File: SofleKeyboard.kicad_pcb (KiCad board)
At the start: 2 copper layers, 143.5 x 111.7 mm, 84 parts, among them J3 OLED, SW1 SW_PUSH_LED, SW10 SW_PUSH_LED, SW11 SW_PUSH_LED, SW12 SW_PUSH_LED, SW13 SW_PUSH_LED, SW14 SW_PUSH_LED, SW15 SW_PUSH_LED, SW16 SW_PUSH_LED, SW17 SW_PUSH_LED, SW18 SW_PUSH_LED, SW19 SW_PUSH_LED, SW2 SW_PUSH_LED, SW20 SW_PUSH_LED, SW21 SW_PUSH_LED, SW22 SW_PUSH_LED, SW23 SW_PUSH_LED, SW24 SW_PUSH_LED, SW26 SW_PUSH_LED, SW27 SW_PUSH_LED, SW28 SW_PUSH_LED, SW29 SW_PUSH_LED, SW3 SW_PUSH_LED, SW30 SW_PUSH_LED, SW4 SW_PUSH_LED, SW5 SW_PUSH_LED, SW6 SW_PUSH_LED, SW7 SW_PUSH_LED, SW8 SW_PUSH_LED, SW9 SW_PUSH_LED, U1 ProMicro

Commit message: update diode footprint, add ground zones, start board routing
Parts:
- D1, D10, D11, D12, D13, D14, D15, D16, D17, D18, D19, D2, D20, D21, D22, D23, D24, D26, D27, D28, D29, D3, D30, D4, D5, D6, D7, D8, D9: footprint Diode_SMD:crkbd-diode -> SofleChoc:crkbd-diode
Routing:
- net row0: track 0.00 -> 187.0 mm, vias 0 -> 6
- net row1: track 0.00 -> 177.8 mm, vias 0 -> 7
- net row4: track 0.00 -> 175.4 mm, vias 0 -> 6
- net Net-(SW_BATT+1-A): track 0.00 -> 111.1 mm, vias 0 -> 2
- net row2: track 0.00 -> 69.4 mm, vias 0 -> 1
- net row3: track 0.00 -> 69.0 mm, vias 0 -> 1
- net col6: track 0.00 -> 66.5 mm, vias 0 -> 1
- net ENCA: track 0.00 -> 64.9 mm, vias 0 -> 1
- net GND: track 0.00 -> 62.4 mm
- net ENCB: track 0.00 -> 61.7 mm, vias 0 -> 1
- net RESET: track 0.00 -> 60.1 mm, vias 0 -> 1
- net CS: track 0.00 -> 54.7 mm, vias 0 -> 5
- net SDA: track 0.00 -> 46.6 mm, vias 0 -> 4
- net SCL: track 0.00 -> 38.0 mm, vias 0 -> 3
- net VCC: track 0.00 -> 35.3 mm, vias 0 -> 1
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- added copper zone on B.Cu, net GND
- added copper zone on F.Cu, net GND

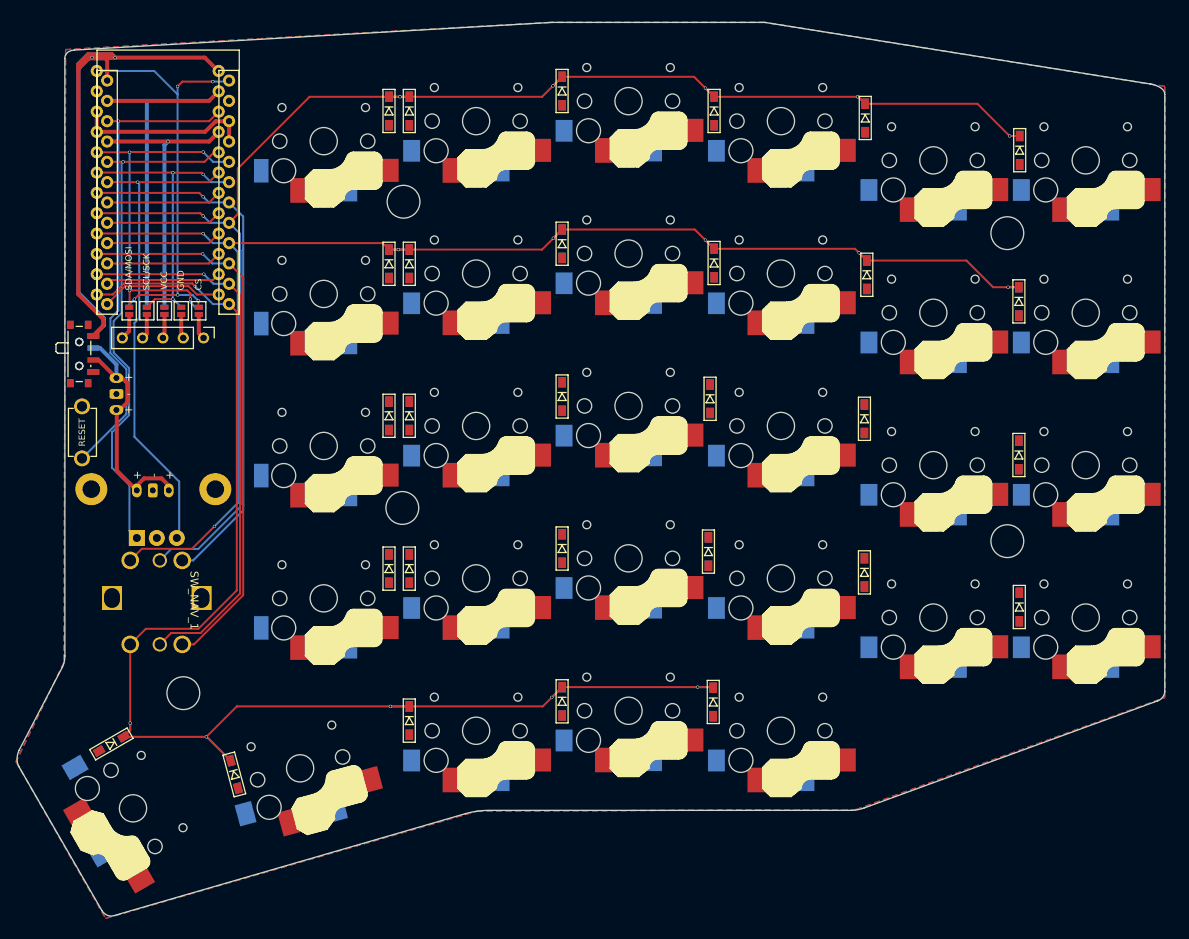
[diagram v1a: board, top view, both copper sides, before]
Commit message: wire columns 5, 4, 3 and 2
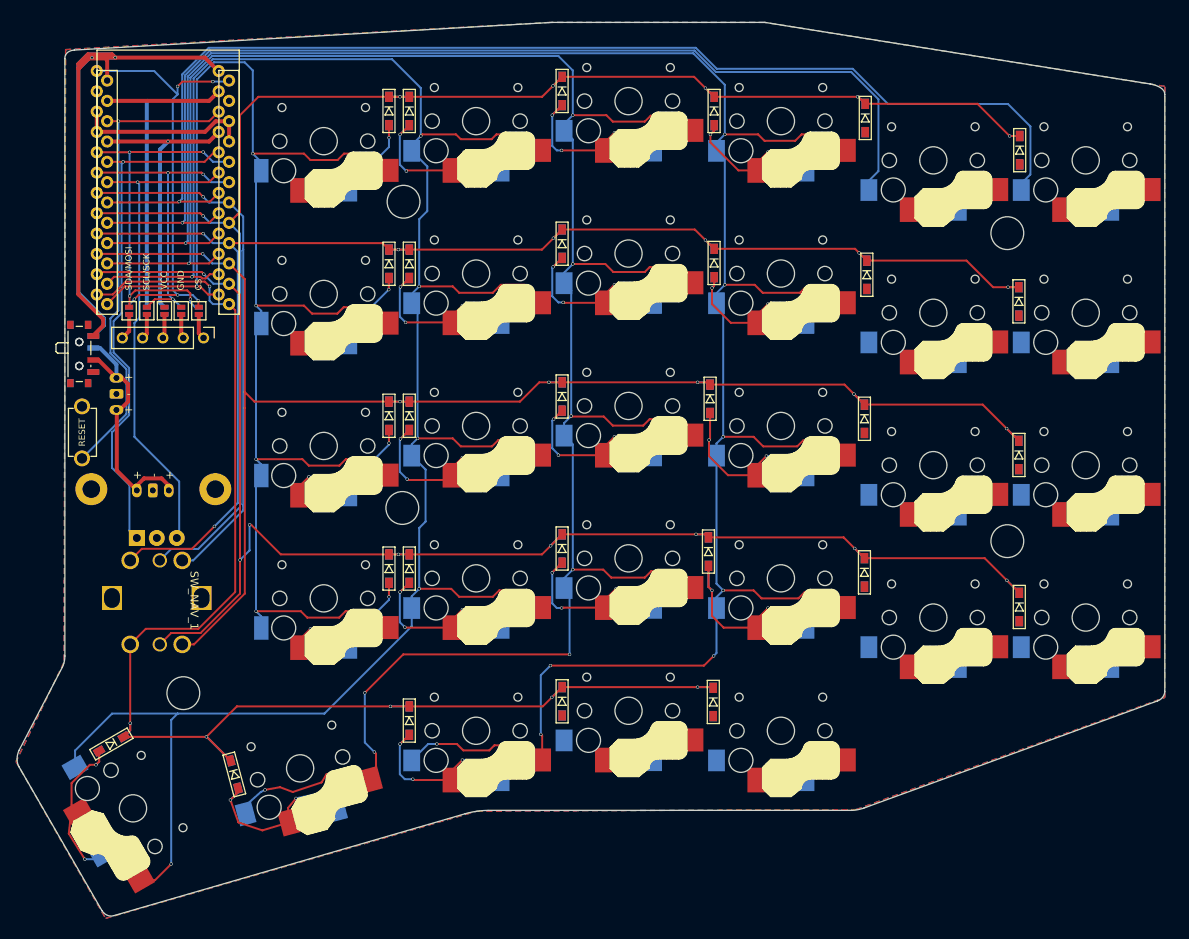
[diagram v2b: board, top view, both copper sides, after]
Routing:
- net col2: track 14.4 -> 298.8 mm, vias 0 -> 9
- net col3: track 14.4 -> 289.2 mm, vias 0 -> 9
- net col4: track 14.4 -> 283.9 mm, vias 0 -> 6
- net col5: track 15.3 -> 194.6 mm, vias 0 -> 5
- net col0: track 14.4 -> 150.4 mm, vias 0 -> 1
- net col1: track 14.4 -> 135.3 mm, vias 0 -> 1
- net row3: track 69.0 -> 186.1 mm, vias 1 -> 8
- net row2: track 69.4 -> 181.3 mm, vias 1 -> 6
- net Net-(D16-A): track 0.00 -> 25.1 mm, vias 0 -> 2
- net Net-(D22-A): track 0.00 -> 25.1 mm, vias 0 -> 2
- net Net-(D28-A): track 0.00 -> 23.4 mm, vias 0 -> 3
- net Net-(D14-A): track 0.00 -> 23.4 mm, vias 0 -> 3
- net Net-(D21-A): track 0.00 -> 23.2 mm, vias 0 -> 3
- net Net-(D2-A): track 0.00 -> 23.0 mm, vias 0 -> 3
- net Net-(D3-A): track 0.00 -> 23.0 mm, vias 0 -> 3
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
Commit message: first iteration done
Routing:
- net col1: track 135.3 -> 314.3 mm, vias 1 -> 9
- net col0: track 150.4 -> 325.1 mm, vias 1 -> 7
- net Net-(D23-A): track 0.00 -> 30.3 mm, vias 0 -> 2
- net Net-(D17-A): track 0.00 -> 30.2 mm, vias 0 -> 2
- net Net-(D5-A): track 0.00 -> 29.2 mm, vias 0 -> 2
- net Net-(D11-A): track 0.00 -> 27.7 mm, vias 0 -> 2
- net Net-(D30-A): track 0.00 -> 24.2 mm, vias 0 -> 2
- net Net-(D29-A): track 0.00 -> 24.0 mm, vias 0 -> 3
- net Net-(D18-A): track 0.00 -> 20.8 mm, vias 0 -> 2
- net Net-(D12-A): track 0.00 -> 20.8 mm, vias 0 -> 2
- net Net-(D6-A): track 0.00 -> 20.8 mm, vias 0 -> 2
- net Net-(D24-A): track 0.00 -> 20.5 mm, vias 0 -> 2
- net GND: track 62.4 -> 79.1 mm, vias 0 -> 9
- net Net-(J3-Pin_1): track 3.30 -> 6.60 mm
- net Net-(J3-Pin_5): track 3.20 -> 6.39 mm
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
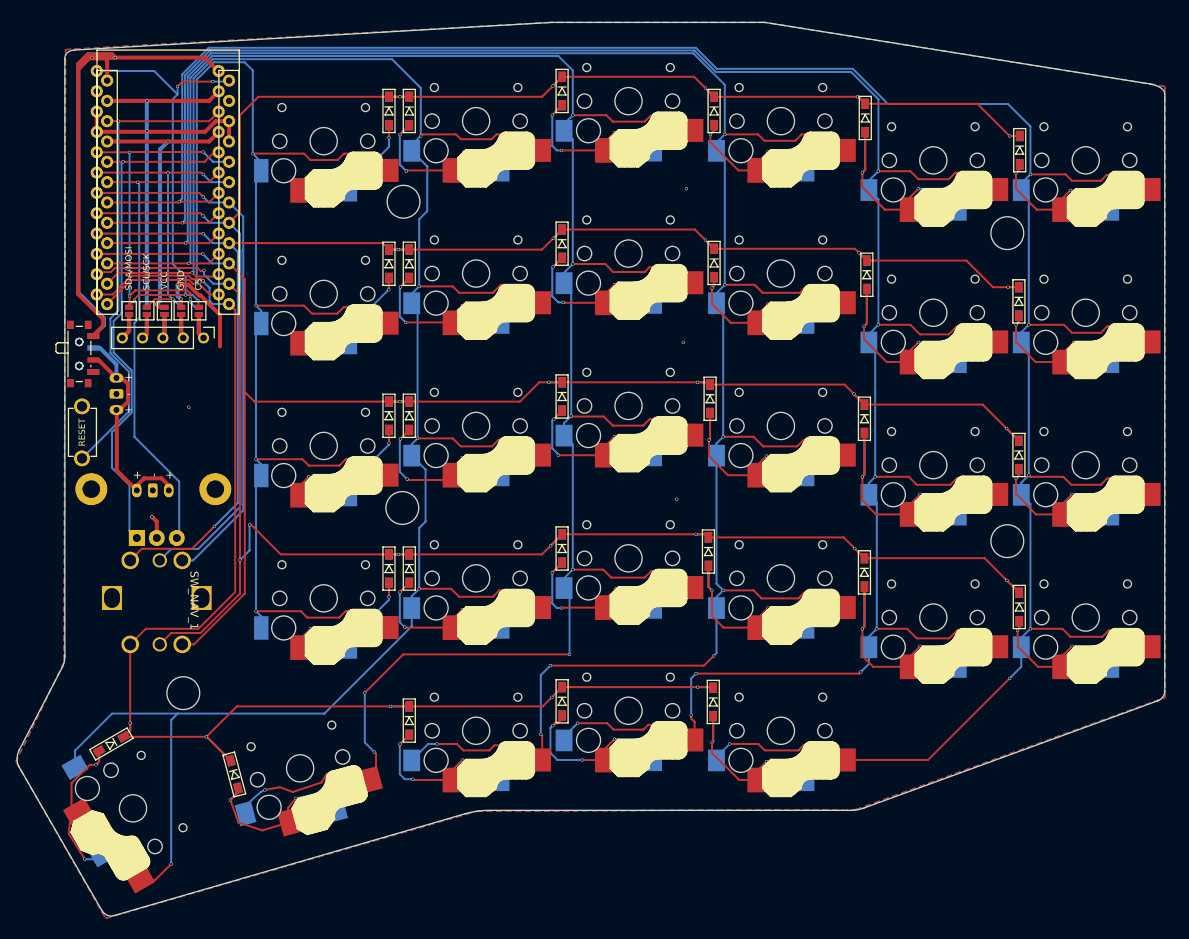
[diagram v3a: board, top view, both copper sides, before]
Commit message: add license
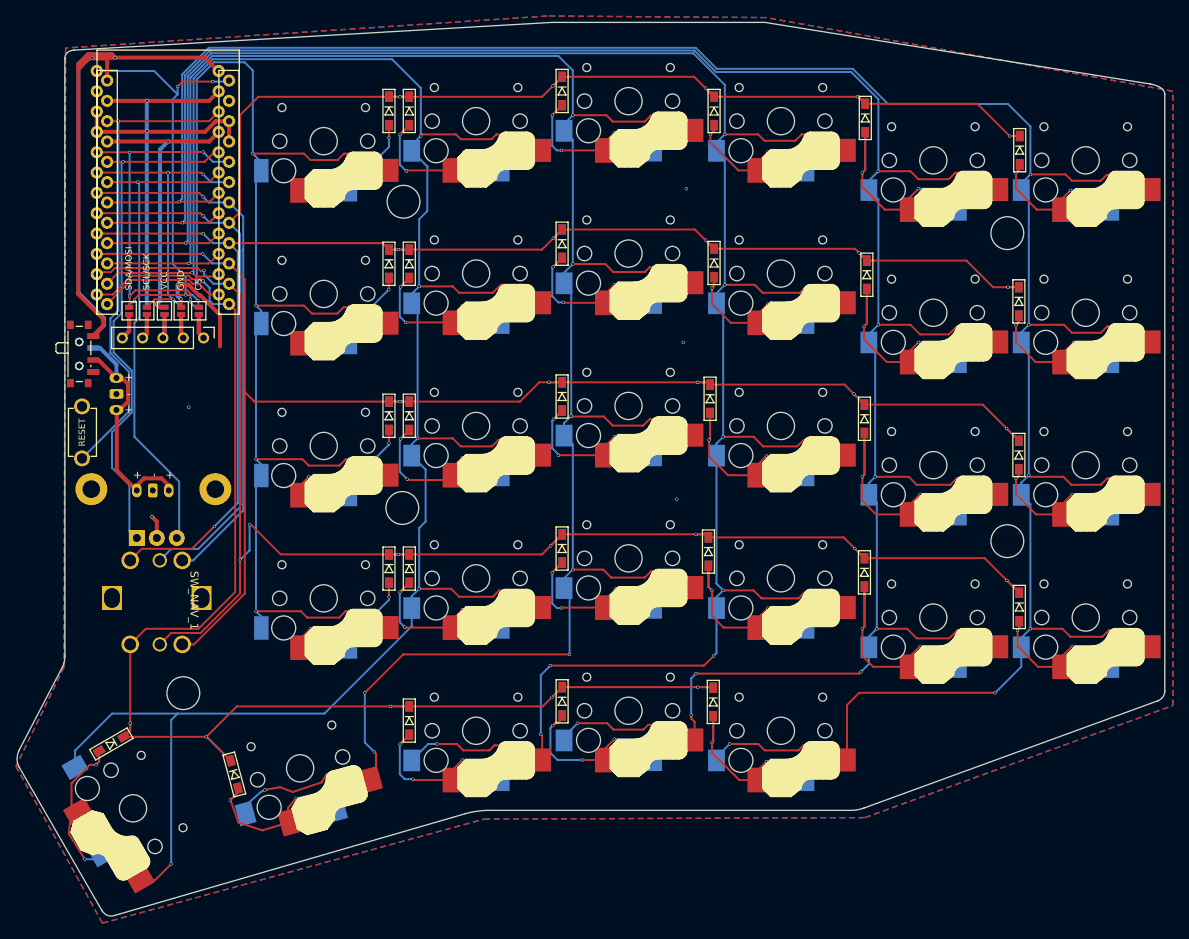
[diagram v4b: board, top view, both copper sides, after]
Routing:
- net col0: track 325.1 -> 329.1 mm
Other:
- rule pad_to_mask_clearance: 0.2 -> 0
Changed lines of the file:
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@@
 			(dielectric_constraints no)
 		)
-		(pad_to_mask_clearance 0.2)
+		(pad_to_mask_clearance 0)
 		(allow_soldermask_bridges_in_footprints no)
 		(tenting front back)
 		(grid_origin 150.33912 99.10264)
 		(pcbplotparams
-			(layerselection 0x00000000_00000000_55555555_575555ff)
+			(layerselection 0x00000000_00000000_55555555_5755f5ff)
 			(plot_on_all_layers_selection 0x00000000_00000000_00000000_00000000)
 			(disableapertmacros no)
@@
 			(drillshape 0)
 			(scaleselection 1)
-			(outputdirectory "../../Gerbers/SofleChocWireless/")
+			(outputdirectory "../BoringSofle-Gerbers/")
 		)
 	)
@@
 	)
 	(segment
+		(start 269.13912 70.90264)
+		(end 252.13912 70.90264)
+		(width 0.25)
+		(layer "F.Cu")
+		(net 2)
+	)
+	(segment
 		(start 278.53912 63.90264)
 		(end 282.53912 63.90264)
@@
 	)
 	(segment
-		(start 260.745126 79.296634)
-		(end 250.610573 79.296634)
-		(width 0.25)
-		(layer "F.Cu")
-		(net 2)
-	)
-	(segment
 		(start 282.33912 6.90264)
 		(end 283.075126 6.166634)
@@
 	)
 	(segment
+		(start 250.610573 72.431187)
+		(end 250.610573 79.296634)
+		(width 0.25)
+		(layer "F.Cu")
+		(net 2)
+	)
+	(segment
 		(start 158.134388 9.612379)
 		(end 167.029381 9.612379)
@@
 	)
 	(segment
-		(start 270.93912 69.10264)
-		(end 260.745126 79.296634)
-		(width 0.25)
-		(layer "F.Cu")
-		(net 2)
-	)
-	(segment
 		(start 167.029381 9.612379)
 		(end 167.13912 9.50264)
@@
 	)
 	(segment
+		(start 252.13912 70.90264)
+		(end 250.610573 72.431187)
+		(width 0.25)
+		(layer "F.Cu")
+		(net 2)
+	)
+	(segment
 		(start 286.880573 6.166634)
 		(end 288.710573 7.996634)
@@
 	)
 	(via
-		(at 270.93912 69.10264)
+		(at 269.13912 70.90264)
 		(size 0.4)
 		(drill 0.3)
@@
 	)
 	(segment
-		(start 272.400573 67.641187)
-		(end 270.93912 69.10264)
-		(width 0.25)
-		(layer "B.Cu")
-		(net 2)
-	)
-	(segment
-		(start 272.400573 65.206634)
-		(end 272.400573 67.641187)
-		(width 0.25)
-		(layer "B.Cu")
-		(net 2)
-	)
-	(segment
 		(start 272.400573 44.641187)
 		(end 273.33912 43.70264)
@@
 	)
 	(segment
+		(start 272.400573 67.641187)
+		(end 272.400573 65.206634)
+		(width 0.25)
+		(layer "B.Cu")
+		(net 2)
+	)
+	(segment
 		(start 273.33912 28.045181)
 		(end 273.33912 43.70264)
@@
 	)
 	(segment
+		(start 269.13912 70.90264)
+		(end 272.400573 67.641187)
+		(width 0.25)
+		(layer "B.Cu")
+		(net 2)
+	)
+	(segment
 		(start 273.53912 47.295181)
 		(end 273.53912 62.90264)
@@
 		(polygon
 			(pts
-				(xy 152.93912 -9.49736) (xy 152.73912 67.10264) (xy 146.73912 79.50264) (xy 157.93912 99.10264)
-				(xy 204.33912 85.70264) (xy 251.73912 85.50264) (xy 290.33912 71.50264) (xy 290.33912 -4.89736)
-				(xy 240.33912 -12.89736) (xy 213.53912 -12.89736)
+				(xy 152.93912 -9.69736) (xy 152.73912 67.70264) (xy 146.73912 80.10264) (xy 157.53912 99.70264)
+				(xy 205.26481 86.693511) (xy 252.86481 86.50264) (xy 291.33912 72.50264) (xy 291.33912 -4.29736)
+				(xy 240.53912 -13.49736) (xy 213.13912 -13.69736)
 			)
 		)

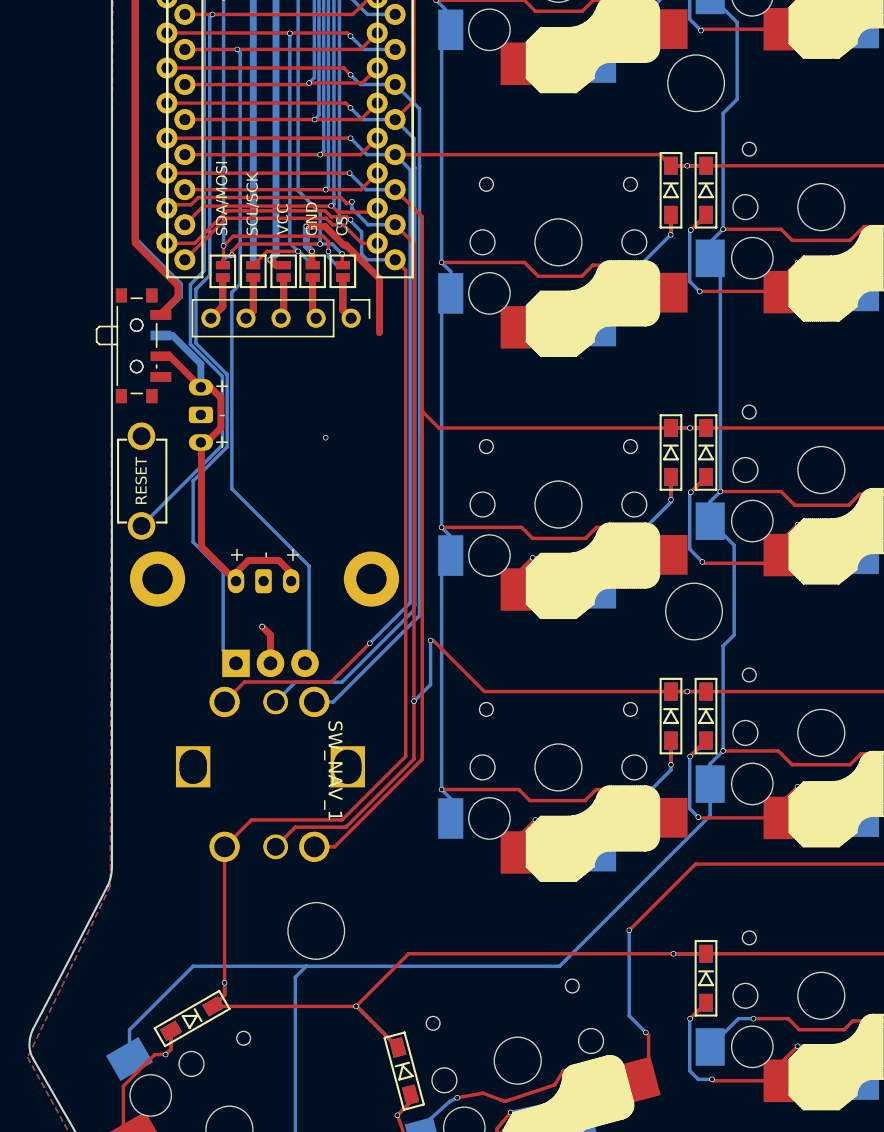
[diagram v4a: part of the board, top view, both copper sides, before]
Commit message: change pushbutton footprint, misc changes
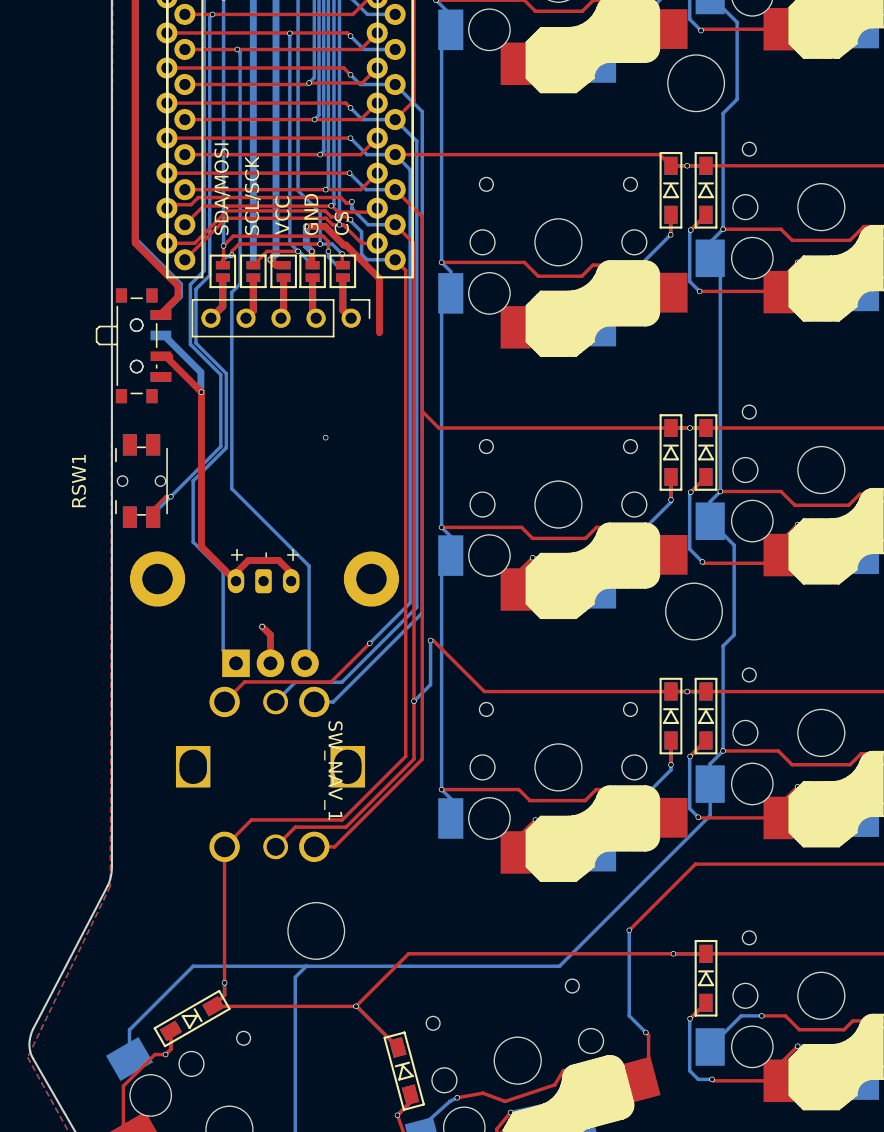
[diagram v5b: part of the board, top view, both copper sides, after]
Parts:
- removed JST_BATT2: Conn_01x02, SofleChoc:JST_PH_S2B-PH-K_1x02_P2.00mm_DoubleSided
- RSW1: footprint SofleKeyboard-footprint:TACT_SWITCH_TVBP06 -> VicoKeyboard:Panasonic_EVQPUL_EVQPUC
- turned RSW1 to 90 degrees
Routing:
- net Net-(JST_BATT1-Pin_2): track 32.2 -> 30.8 mm, vias 0 -> 1
- net RESET: track 60.4 -> 61.5 mm, vias 1 -> 2
